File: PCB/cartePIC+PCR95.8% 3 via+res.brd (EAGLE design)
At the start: 100 x 80 mm, 19 parts, among them IC1 4511N, IC2 4511N, IC3 PIC16F877P

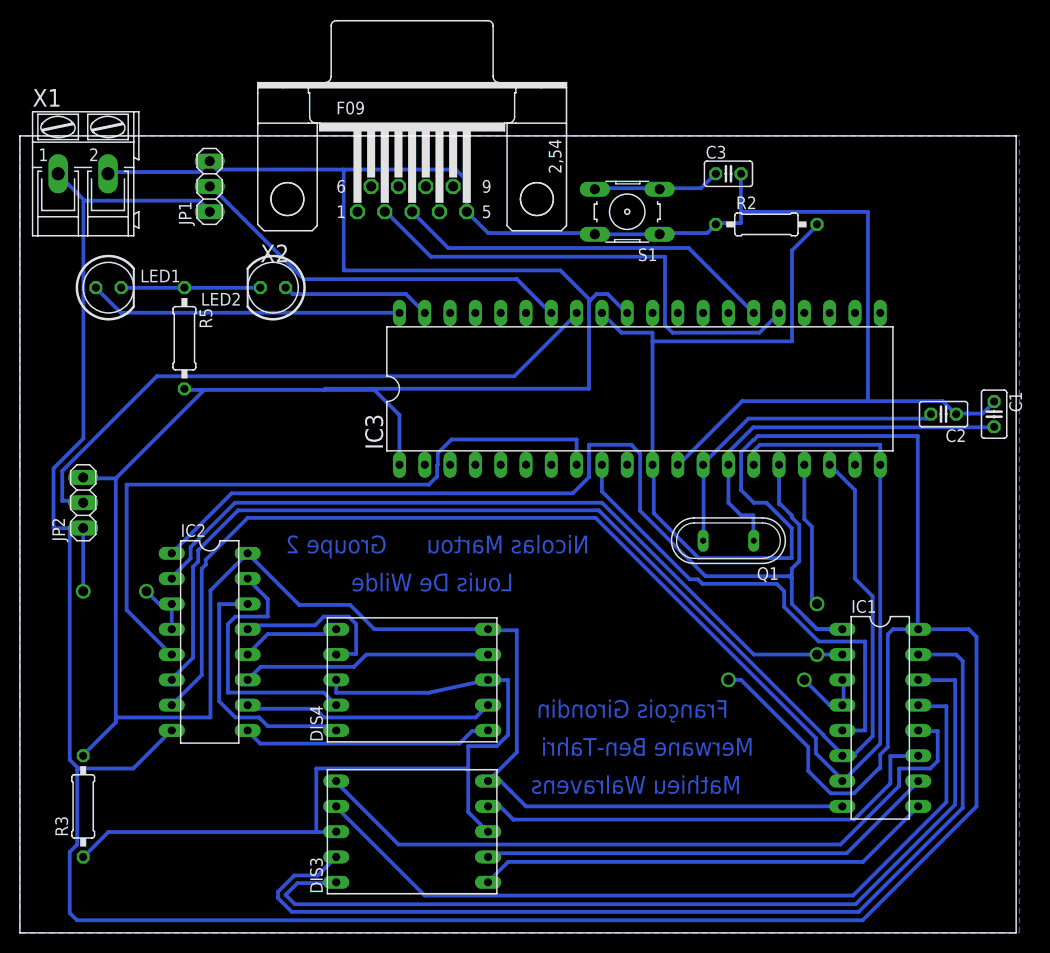
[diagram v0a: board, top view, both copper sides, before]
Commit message: correction erreur nom groupe + vertion avec resistance
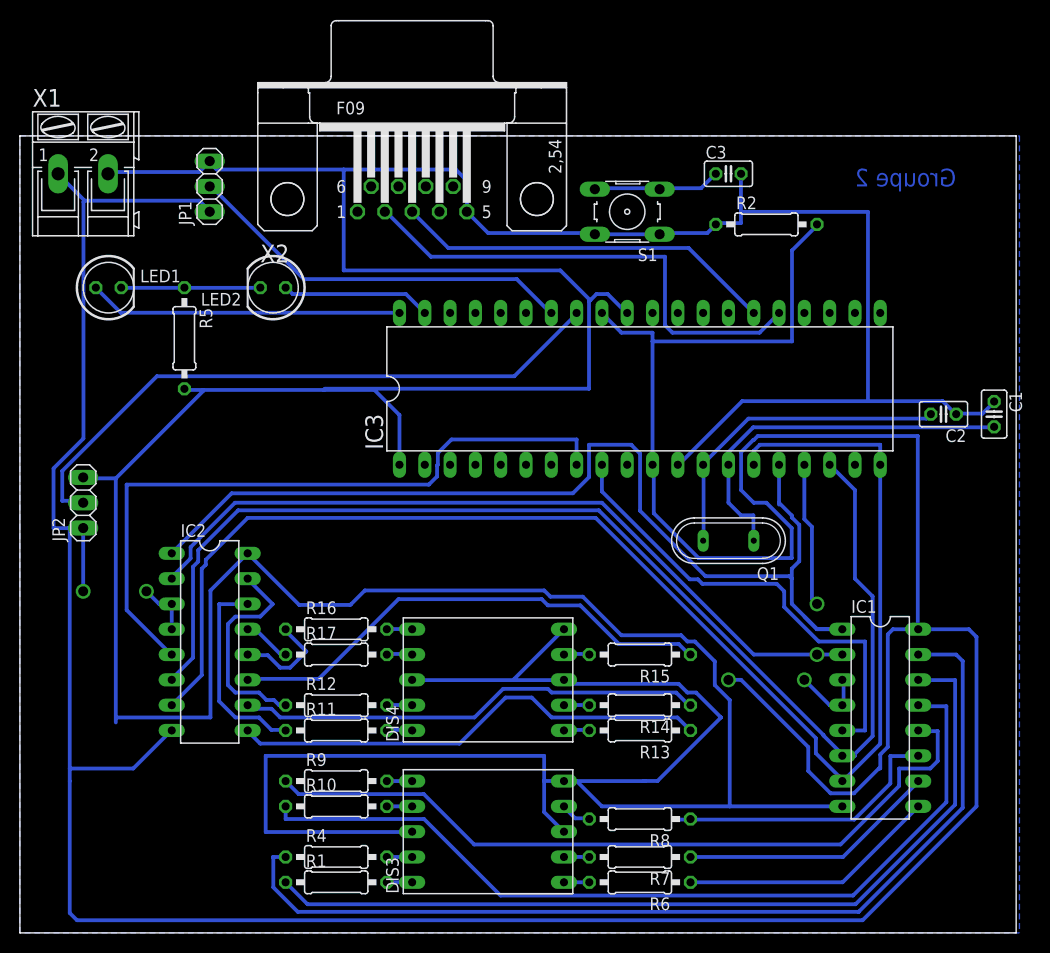
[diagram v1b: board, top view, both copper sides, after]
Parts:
- removed R3: (no value), rcl:0207/10
- added R1, R10, R11, R12, R13, R14, R15, R16, R17, R4, R6, R7, R8, R9: (no value), rcl:0207/10
- moved DIS3 7.62 mm to (47.0, 10.2)
- moved DIS4 7.62 mm to (47.0, 25.4)
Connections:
- removed net N$23: DIS3.3, DIS3.8, DIS4.3, DIS4.8, R3.1
- new net N$32: DIS3.10, R1.2
- new net N$33: DIS3.9, R4.2
- new net N$34: DIS3.1, R6.2
- new net N$35: DIS3.2, R7.2
- new net N$36: DIS3.4, R8.2
- new net N$37: DIS3.6, R9.2
- new net N$38: DIS3.7, R10.2
- new net N$39: DIS4.10, R11.2
- new net N$40: DIS4.9, R12.2
- new net N$41: DIS4.1, R13.2
- new net N$42: DIS4.2, R14.2
- new net N$43: DIS4.4, R15.2
- new net N$44: DIS4.6, R16.2
- new net N$45: DIS4.7, R17.2
- net GND: now also DIS3.3, DIS3.8, DIS4.3, DIS4.8; no longer R3.2
- net N$10: now also R4.1; no longer DIS3.9
- net N$11: now also R6.1; no longer DIS3.1
- net N$12: now also R7.1; no longer DIS3.2
- net N$13: now also R8.1; no longer DIS3.4
- net N$14: now also R9.1; no longer DIS3.6
- net N$15: now also R10.1; no longer DIS3.7
- net N$16: now also R11.1; no longer DIS4.10
- net N$17: now also R12.1; no longer DIS4.9
- net N$18: now also R13.1; no longer DIS4.1
- net N$19: now also R14.1; no longer DIS4.2
- net N$20: now also R15.1; no longer DIS4.4
- net N$21: now also R16.1; no longer DIS4.6
- net N$22: now also R17.1; no longer DIS4.7
- net N$9: now also R1.1; no longer DIS3.10
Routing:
- net GND: track 402.3 -> 528.7 mm
- net N$23: track 86.2 -> 0.00 mm
- net N$20: track 25.2 -> 50.2 mm
- net N$18: track 25.2 -> 48.3 mm
- net N$19: track 25.2 -> 47.4 mm
- net N$11: track 46.4 -> 26.0 mm
- net N$12: track 46.4 -> 26.0 mm
- net N$13: track 48.0 -> 28.6 mm
- net N$22: track 16.8 -> 5.60 mm
- net N$15: track 81.4 -> 87.2 mm
- net N$17: track 27.2 -> 21.7 mm
- net N$9: track 93.6 -> 88.5 mm
- net N$16: track 25.6 -> 20.5 mm
- net N$14: track 72.6 -> 77.6 mm
- net N$36: track 0.00 -> 3.12 mm
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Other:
- board text removed: "François Girondin"
- board text removed: "Louis De Wilde"
- board text removed: "Mathieu Walravens"
- board text removed: "Merwane Ben-Tahri"
- board text removed: "Nicolas Martou"
